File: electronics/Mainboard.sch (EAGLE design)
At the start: 225 parts, among them J1 JST_PH_B3B-PH-K-S(LF)(SN), J10 JST_PH_B3B-PH-K-S(LF)(SN), J11 JST_PH_B3B-PH-K-S(LF)(SN), J12 JST_PH_B3B-PH-K-S(LF)(SN), J13 JST_PH_B3B-PH-K-S(LF)(SN), J14 JST_PH_B3B-PH-K-S(LF)(SN), J15 JST_PH_B3B-PH-K-S(LF)(SN), J16 JST_PH_B3B-PH-K-S(LF)(SN), J17 JST_PH_B3B-PH-K-S(LF)(SN), J18 JST_PH_B3B-PH-K-S(LF)(SN), J19 JST_PH_B3B-PH-K-S(LF)(SN), J2 JST_PH_B3B-PH-K-S(LF)(SN), J20 JST_PH_B3B-PH-K-S(LF)(SN), J21 JST_PH_B3B-PH-K-S(LF)(SN), J22 JST_PH_B3B-PH-K-S(LF)(SN), J23 JST_PH_B3B-PH-K-S(LF)(SN), J24 JST_PH_B3B-PH-K-S(LF)(SN), J25 JST_PH_B3B-PH-K-S(LF)(SN), J26 JST_PH_B3B-PH-K-S(LF)(SN), J27 JST_PH_B3B-PH-K-S(LF)(SN), J28 JST_PH_B3B-PH-K-S(LF)(SN), J29 JST_PH_B3B-PH-K-S(LF)(SN), J3 JST_PH_B3B-PH-K-S(LF)(SN), J30 JST_PH_B3B-PH-K-S(LF)(SN), J31 JST_PH_B3B-PH-K-S(LF)(SN), J32 JST_PH_B3B-PH-K-S(LF)(SN), J33 B4B-PH-K-S(LF)(SN), J34 B4B-PH-K-S(LF)(SN), J35 B4B-PH-K-S(LF)(SN), J36 B4B-PH-K-S(LF)(SN), J37 B4B-PH-K-S(LF)(SN), J38 B4B-PH-K-S(LF)(SN), J39 B4B-PH-K-S(LF)(SN), J4 JST_PH_B3B-PH-K-S(LF)(SN), J40 B4B-PH-K-S(LF)(SN), J41 B4B-PH-K-S(LF)(SN), J42 B4B-PH-K-S(LF)(SN), J43 B4B-PH-K-S(LF)(SN), J44 B4B-PH-K-S(LF)(SN), J45 B4B-PH-K-S(LF)(SN), J46 B4B-PH-K-S(LF)(SN), J47 B4B-PH-K-S(LF)(SN), J48 B4B-PH-K-S(LF)(SN), J49 B4B-PH-K-S(LF)(SN), J5 JST_PH_B3B-PH-K-S(LF)(SN), J50 B4B-PH-K-S(LF)(SN), J51 B4B-PH-K-S(LF)(SN), J52 B4B-PH-K-S(LF)(SN), J53 B4B-PH-K-S(LF)(SN), J54 B4B-PH-K-S(LF)(SN), J55 B4B-PH-K-S(LF)(SN), J56 B4B-PH-K-S(LF)(SN), J57 B4B-PH-K-S(LF)(SN), J58 B4B-PH-K-S(LF)(SN), J59 B4B-PH-K-S(LF)(SN), J6 JST_PH_B3B-PH-K-S(LF)(SN), J60 B4B-PH-K-S(LF)(SN), J61 B4B-PH-K-S(LF)(SN), J62 B4B-PH-K-S(LF)(SN), J63 B4B-PH-K-S(LF)(SN), J64 B4B-PH-K-S(LF)(SN), J7 JST_PH_B3B-PH-K-S(LF)(SN), J8 JST_PH_B3B-PH-K-S(LF)(SN), J9 JST_PH_B3B-PH-K-S(LF)(SN), U1 AMP-5103309-7-34PIN_5103309-7, U15 AD5360BSTZ, U16 ADR425ARZ, U18 AD7730BRUZ, U19 AD5360BSTZ, U2 AMP-5103309-7-34PIN_5103309-7, U20 ADR425ARZ, U21 AD7730BRUZ, U22 STM32F103RCT6, U23 AD7730BRUZ, U24 AD7730BRUZ, U25 AD7730BRUZ, U26 AD7730BRUZ, U27 AD7730BRUZ, U28 AD7730BRUZ, U38 AD7730BRUZ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

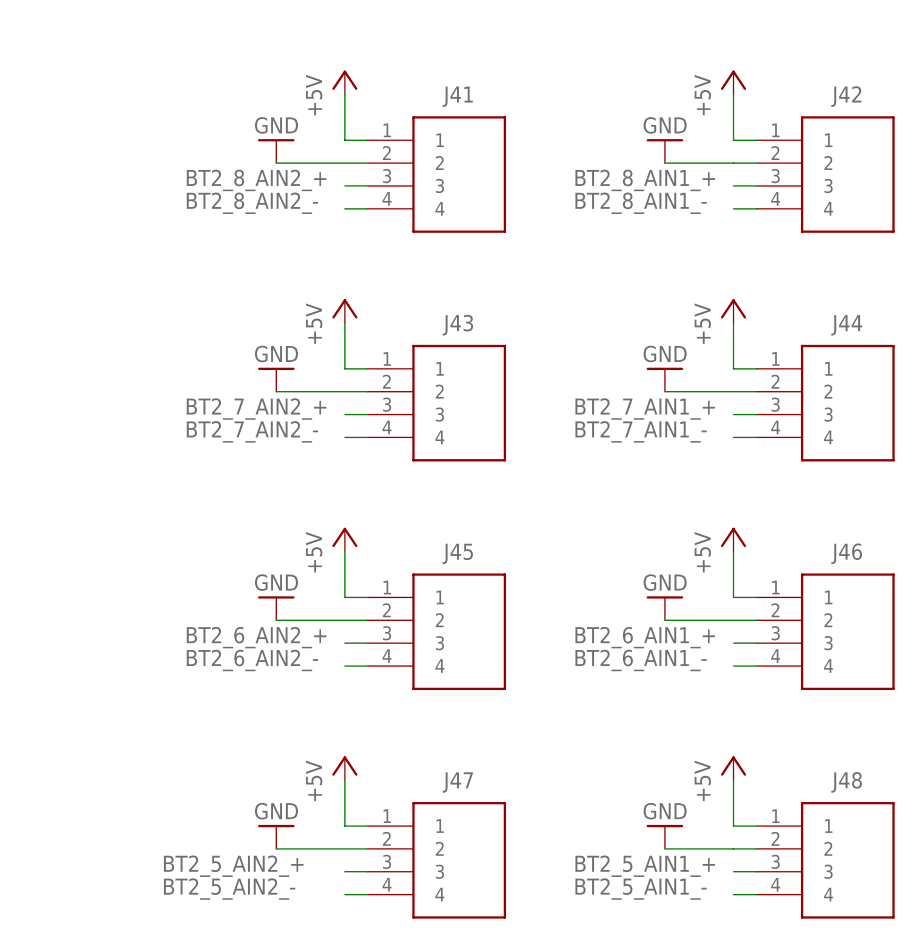
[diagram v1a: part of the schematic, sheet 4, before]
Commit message: reworked second load cell section
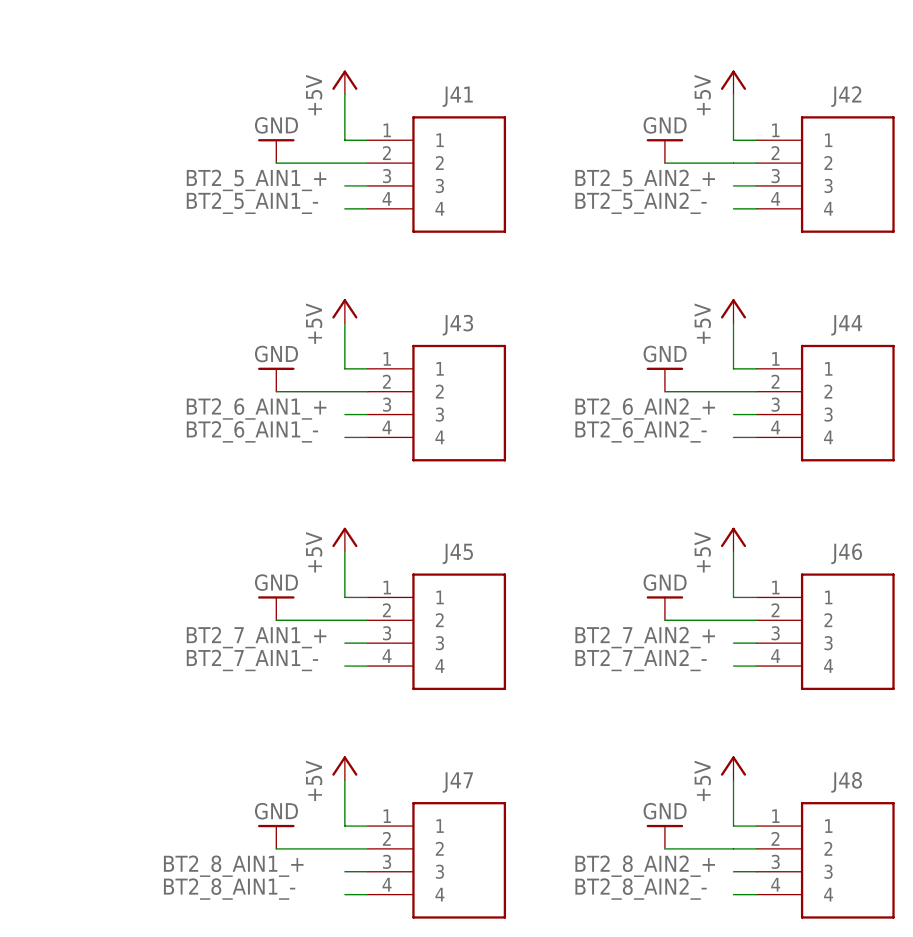
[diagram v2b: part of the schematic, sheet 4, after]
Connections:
- net N$109 renamed LC2_OSC_IN
- net N$110 renamed LC2_OSC_OUT
- net BT2_5_AIN1_+: now also J41.3; no longer J48.3
- net BT2_5_AIN1_-: now also J41.4; no longer J48.4
- net BT2_5_AIN2_+: now also J42.3; no longer J47.3
- net BT2_5_AIN2_-: now also J42.4; no longer J47.4
- net BT2_6_AIN1_+: now also J43.3; no longer J46.3
- net BT2_6_AIN1_-: now also J43.4; no longer J46.4
- net BT2_6_AIN2_+: now also J44.3; no longer J45.3
- net BT2_6_AIN2_-: now also J44.4; no longer J45.4
- net BT2_7_AIN1_+: now also J45.3; no longer J44.3
- net BT2_7_AIN1_-: now also J45.4; no longer J44.4
- net BT2_7_AIN2_+: now also J46.3; no longer J43.3
- net BT2_7_AIN2_-: now also J46.4; no longer J43.4
- net BT2_8_AIN1_+: now also J47.3; no longer J42.3
- net BT2_8_AIN1_-: now also J47.4; no longer J42.4
- net BT2_8_AIN2_+: now also J48.3; no longer J41.3
- net BT2_8_AIN2_-: now also J48.4; no longer J41.4
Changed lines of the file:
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@@
 <wire x1="121.92" y1="127" x2="129.54" y2="127" width="0.1524" layer="91"/>
 <wire x1="121.92" y1="129.54" x2="114.3" y2="129.54" width="0.1524" layer="91"/>
-<label x="73.66" y="129.54" size="1.778" layer="95"/>
+<label x="81.28" y="129.54" size="1.778" layer="95"/>
 <pinref part="C13" gate="G$1" pin="1"/>
 <wire x1="114.3" y1="129.54" x2="104.14" y2="129.54" width="0.1524" layer="91"/>
@@
 <pinref part="U22" gate="A" pin="VDDA"/>
 <wire x1="129.54" y1="137.16" x2="111.76" y2="137.16" width="0.1524" layer="91"/>
-<label x="91.44" y="137.16" size="1.778" layer="95"/>
+<label x="99.06" y="137.16" size="1.778" layer="95"/>
 <pinref part="C12" gate="G$1" pin="2"/>
 <wire x1="111.76" y1="137.16" x2="99.06" y2="137.16" width="0.1524" layer="91"/>
@@
 <wire x1="767.08" y1="137.16" x2="774.7" y2="137.16" width="0.1524" layer="91"/>
 <wire x1="767.08" y1="139.7" x2="759.46" y2="139.7" width="0.1524" layer="91"/>
-<label x="718.82" y="139.7" size="1.778" layer="95"/>
+<label x="726.44" y="139.7" size="1.778" layer="95"/>
 <pinref part="C54" gate="G$1" pin="1"/>
 <wire x1="759.46" y1="139.7" x2="749.3" y2="139.7" width="0.1524" layer="91"/>
@@
 <pinref part="U40" gate="A" pin="VDDA"/>
 <wire x1="774.7" y1="147.32" x2="756.92" y2="147.32" width="0.1524" layer="91"/>
-<label x="736.6" y="147.32" size="1.778" layer="95"/>
+<label x="744.22" y="147.32" size="1.778" layer="95"/>
 <pinref part="C53" gate="G$1" pin="2"/>
 <wire x1="756.92" y1="147.32" x2="744.22" y2="147.32" width="0.1524" layer="91"/>
@@
 </segment>
 </net>
-<net name="N$109" class="0">
+<net name="LC2_OSC_IN" class="0">
 <segment>
 <pinref part="Y8" gate="G$1" pin="OSC1"/>
@@
 <pinref part="C59" gate="G$1" pin="1"/>
 <wire x1="873.76" y1="154.94" x2="886.46" y2="154.94" width="0.1524" layer="91"/>
+<label x="835.66" y="142.24" size="1.778" layer="95"/>
 </segment>
 </net>
-<net name="N$110" class="0">
+<net name="LC2_OSC_OUT" class="0">
 <segment>
 <pinref part="Y8" gate="G$1" pin="OSC2"/>
@@
 <wire x1="904.24" y1="129.54" x2="904.24" y2="137.16" width="0.1524" layer="91"/>
 <junction x="904.24" y="137.16"/>
+<label x="835.66" y="139.7" size="1.778" layer="95"/>
 </segment>
 </net>
@@
 </segment>
 </net>
-<net name="BT2_8_AIN1_+" class="0">
-<segment>
-<pinref part="J42" gate="G$1" pin="3"/>
-<wire x1="345.44" y1="78.74" x2="342.9" y2="78.74" width="0.1524" layer="91"/>
-<label x="325.12" y="78.74" size="1.778" layer="95"/>
-</segment>
-</net>
-<net name="BT2_8_AIN1_-" class="0">
-<segment>
-<pinref part="J42" gate="G$1" pin="4"/>
-<wire x1="345.44" y1="76.2" x2="342.9" y2="76.2" width="0.1524" layer="91"/>
-<label x="325.12" y="76.2" size="1.778" layer="95"/>
-</segment>
-</net>
-<net name="BT2_8_AIN2_+" class="0">
-<segment>
-<pinref part="J41" gate="G$1" pin="3"/>
-<wire x1="302.26" y1="78.74" x2="299.72" y2="78.74" width="0.1524" layer="91"/>
-<label x="281.94" y="78.74" size="1.778" layer="95"/>
-</segment>
-</net>
-<net name="BT2_8_AIN2_-" class="0">
-<segment>
-<pinref part="J41" gate="G$1" pin="4"/>
-<wire x1="302.26" y1="76.2" x2="299.72" y2="76.2" width="0.1524" layer="91"/>
-<label x="281.94" y="76.2" size="1.778" layer="95"/>
-</segment>
-</net>
-<net name="BT2_7_AIN2_+" class="0">
-<segment>
-<pinref part="J43" gate="G$1" pin="3"/>
-<wire x1="302.26" y1="53.34" x2="299.72" y2="53.34" width="0.1524" layer="91"/>
-<label x="281.94" y="53.34" size="1.778" layer="95"/>
-</segment>
-</net>
-<net name="BT2_7_AIN2_-" class="0">
-<segment>
-<pinref part="J43" gate="G$1" pin="4"/>
-<wire x1="302.26" y1="50.8" x2="299.72" y2="50.8" width="0.1524" layer="91"/>
-<label x="281.94" y="50.8" size="1.778" layer="95"/>
-</segment>
-</net>
 <net name="BT2_6_AIN2_+" class="0">
 <segment>
-<pinref part="J45" gate="G$1" pin="3"/>
-<wire x1="302.26" y1="27.94" x2="299.72" y2="27.94" width="0.1524" layer="91"/>
-<label x="281.94" y="27.94" size="1.778" layer="95"/>
-</segment>
-</net>
-<net name="BT2_6_AIN2_-" class="0">
-<segment>
-<pinref part="J45" gate="G$1" pin="4"/>
-<wire x1="302.26" y1="25.4" x2="299.72" y2="25.4" width="0.1524" layer="91"/>
-<label x="281.94" y="25.4" size="1.778" layer="95"/>
-</segment>
-</net>
-<net name="BT2_7_AIN1_+" class="0">
-<segment>
 <pinref part="J44" gate="G$1" pin="3"/>
 <wire x1="345.44" y1="53.34" x2="342.9" y2="53.34" width="0.1524" layer="91"/>
@@
 </segment>
 </net>
-<net name="BT2_7_AIN1_-" class="0">
+<net name="BT2_6_AIN2_-" class="0">
 <segment>
 <pinref part="J44" gate="G$1" pin="4"/>
@@
 <net name="BT2_6_AIN1_+" class="0">
 <segment>
-<pinref part="J46" gate="G$1" pin="3"/>
-<wire x1="345.44" y1="27.94" x2="342.9" y2="27.94" width="0.1524" layer="91"/>
-<label x="325.12" y="27.94" size="1.778" layer="95"/>
+<pinref part="J43" gate="G$1" pin="3"/>
+<wire x1="302.26" y1="53.34" x2="299.72" y2="53.34" width="0.1524" layer="91"/>
+<label x="281.94" y="53.34" size="1.778" layer="95"/>
 </segment>
 </net>
 <net name="BT2_6_AIN1_-" class="0">
 <segment>
-<pinref part="J46" gate="G$1" pin="4"/>
-<wire x1="345.44" y1="25.4" x2="342.9" y2="25.4" width="0.1524" layer="91"/>
-<label x="325.12" y="25.4" size="1.778" layer="95"/>
+<pinref part="J43" gate="G$1" pin="4"/>
+<wire x1="302.26" y1="50.8" x2="299.72" y2="50.8" width="0.1524" layer="91"/>
+<label x="281.94" y="50.8" size="1.778" layer="95"/>
 </segment>
 </net>
 <net name="BT2_5_AIN2_+" class="0">
 <segment>
-<pinref part="J47" gate="G$1" pin="3"/>
-<wire x1="302.26" y1="2.54" x2="299.72" y2="2.54" width="0.1524" layer="91"/>
-<label x="279.4" y="2.54" size="1.778" layer="95"/>
+<pinref part="J42" gate="G$1" pin="3"/>
+<wire x1="345.44" y1="78.74" x2="342.9" y2="78.74" width="0.1524" layer="91"/>
+<label x="325.12" y="78.74" size="1.778" layer="95"/>
 </segment>
 </net>
 <net name="BT2_5_AIN2_-" class="0">
 <segment>
-<pinref part="J47" gate="G$1" pin="4"/>
-<wire x1="302.26" y1="0" x2="299.72" y2="0" width="0.1524" layer="91"/>
-<label x="279.4" y="0" size="1.778" layer="95"/>
+<pinref part="J42" gate="G$1" pin="4"/>
+<wire x1="345.44" y1="76.2" x2="342.9" y2="76.2" width="0.1524" layer="91"/>
+<label x="325.12" y="76.2" size="1.778" layer="95"/>
 </segment>
 </net>
 <net name="BT2_5_AIN1_+" class="0">
 <segment>
-<pinref part="J48" gate="G$1" pin="3"/>
-<wire x1="345.44" y1="2.54" x2="342.9" y2="2.54" width="0.1524" layer="91"/>
-<label x="325.12" y="2.54" size="1.778" layer="95"/>
+<pinref part="J41" gate="G$1" pin="3"/>
+<wire x1="302.26" y1="78.74" x2="299.72" y2="78.74" width="0.1524" layer="91"/>
+<label x="281.94" y="78.74" size="1.778" layer="95"/>
 </segment>
 </net>
 <net name="BT2_5_AIN1_-" class="0">
 <segment>
-<pinref part="J48" gate="G$1" pin="4"/>
-<wire x1="345.44" y1="0" x2="342.9" y2="0" width="0.1524" layer="91"/>
-<label x="325.12" y="0" size="1.778" layer="95"/>
+<pinref part="J41" gate="G$1" pin="4"/>
+<wire x1="302.26" y1="76.2" x2="299.72" y2="76.2" width="0.1524" layer="91"/>
+<label x="281.94" y="76.2" size="1.778" layer="95"/>
 </segment>
 </net>
@@
 </segment>
 </net>
+<net name="BT2_7_AIN1_+" class="0">
+<segment>
+<pinref part="J45" gate="G$1" pin="3"/>
+<wire x1="302.26" y1="27.94" x2="299.72" y2="27.94" width="0.1524" layer="91"/>
+<label x="281.94" y="27.94" size="1.778" layer="95"/>
+</segment>
+</net>
+<net name="BT2_7_AIN1_-" class="0">
+<segment>
+<pinref part="J45" gate="G$1" pin="4"/>
+<wire x1="302.26" y1="25.4" x2="299.72" y2="25.4" width="0.1524" layer="91"/>
+<label x="281.94" y="25.4" size="1.778" layer="95"/>
+</segment>
+</net>
+<net name="BT2_7_AIN2_-" class="0">
+<segment>
+<pinref part="J46" gate="G$1" pin="4"/>
+<wire x1="345.44" y1="25.4" x2="342.9" y2="25.4" width="0.1524" layer="91"/>
+<label x="325.12" y="25.4" size="1.778" layer="95"/>
+</segment>
+</net>
+<net name="BT2_7_AIN2_+" class="0">
+<segment>
+<pinref part="J46" gate="G$1" pin="3"/>
+<wire x1="345.44" y1="27.94" x2="342.9" y2="27.94" width="0.1524" layer="91"/>
+<label x="325.12" y="27.94" size="1.778" layer="95"/>
+</segment>
+</net>
+<net name="BT2_8_AIN1_+" class="0">
+<segment>
+<pinref part="J47" gate="G$1" pin="3"/>
+<wire x1="302.26" y1="2.54" x2="299.72" y2="2.54" width="0.1524" layer="91"/>
+<label x="279.4" y="2.54" size="1.778" layer="95"/>
+</segment>
+</net>
+<net name="BT2_8_AIN1_-" class="0">
+<segment>
+<pinref part="J47" gate="G$1" pin="4"/>
+<wire x1="302.26" y1="0" x2="299.72" y2="0" width="0.1524" layer="91"/>
+<label x="279.4" y="0" size="1.778" layer="95"/>
+</segment>
+</net>
+<net name="BT2_8_AIN2_+" class="0">
+<segment>
+<pinref part="J48" gate="G$1" pin="3"/>
+<wire x1="345.44" y1="2.54" x2="342.9" y2="2.54" width="0.1524" layer="91"/>
+<label x="325.12" y="2.54" size="1.778" layer="95"/>
+</segment>
+</net>
+<net name="BT2_8_AIN2_-" class="0">
+<segment>
+<pinref part="J48" gate="G$1" pin="4"/>
+<wire x1="345.44" y1="0" x2="342.9" y2="0" width="0.1524" layer="91"/>
+<label x="325.12" y="0" size="1.778" layer="95"/>
+</segment>
+</net>

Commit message: load cell sections done
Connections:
- net LC2_OSC_IN renamed LC_2_OSC_IN
- net LC2_OSC_OUT renamed LC_2_OSC_OUT
- removed net LC_1_RDY8: U22.PA0-WKUP, U28.*RDY
- removed net LC_1_SS1: U18.*CS, U22.PC9
- removed net LC_1_SS2: U21.*CS, U22.PC8
- removed net LC_1_SS3: U22.PC7, U23.*CS
- removed net LC_1_SS4: U22.PC6, U24.*CS
- removed net LC_1_SS5: U22.PC3, U25.*CS
- removed net LC_1_SS6: U22.PC2, U26.*CS
- removed net LC_1_SS7: U22.PC1, U27.*CS
- removed net LC_1_SS8: U22.PC0, U28.*CS
- removed net LC_2_RDY8: U40.PA0-WKUP, U46.*RDY
- removed net LC_2_SS1: U38.*CS, U40.PC9
- removed net LC_2_SS2: U39.*CS, U40.PC8
- removed net LC_2_SS3: U40.PC7, U41.*CS
- removed net LC_2_SS4: U40.PC6, U42.*CS
- removed net LC_2_SS5: U40.PC3, U43.*CS
- removed net LC_2_SS6: U40.PC2, U44.*CS
- removed net LC_2_SS7: U40.PC1, U45.*CS
- removed net LC_2_SS8: U40.PC0, U46.*CS
- new net LC_1_CS0: U18.*CS, U22.PA0-WKUP
- new net LC_1_CS1: U21.*CS, U22.PA1
- new net LC_1_CS2: U22.PA2, U23.*CS
- new net LC_1_CS3: U22.PC4, U24.*CS
- new net LC_1_CS4: U22.PC5, U25.*CS
- new net LC_1_CS5: U22.PB0, U26.*CS
- new net LC_1_CS6: U22.PB1, U27.*CS
- new net LC_1_CS7: U22.PB1_2, U28.*CS
- new net LC_1_PB7: U22.PB7
- new net LC_1_RDY0: U18.*RDY, U22.PA12
- new net LC_2_CS0: U38.*CS, U40.PA0-WKUP
- new net LC_2_CS1: U39.*CS, U40.PA1
- new net LC_2_CS2: U40.PA2, U41.*CS
- new net LC_2_CS3: U40.PC4, U42.*CS
- new net LC_2_CS4: U40.PC5, U43.*CS
- new net LC_2_CS5: U40.PB0, U44.*CS
- new net LC_2_CS6: U40.PB1, U45.*CS
- new net LC_2_CS7: U40.PB1_2, U46.*CS
- new net LC_2_PB7: U40.PB7
- new net LC_2_RDY0: U38.*RDY, U40.PA12
- net LC_1_RDY1: now also U21.*RDY; no longer U18.*RDY
- net LC_1_RDY2: now also U23.*RDY; no longer U21.*RDY
- net LC_1_RDY3: now also U24.*RDY; no longer U23.*RDY
- net LC_1_RDY4: now also U22.PA8, U25.*RDY; no longer U22.PA12, U24.*RDY
- net LC_1_RDY5: now also U22.PC9, U26.*RDY; no longer U22.PA3, U25.*RDY
- net LC_1_RDY6: now also U22.PC8, U27.*RDY; no longer U22.PA2, U26.*RDY
- net LC_1_RDY7: now also U22.PC7, U28.*RDY; no longer U22.PA1, U27.*RDY
- net LC_2_RDY1: now also U39.*RDY; no longer U38.*RDY
- net LC_2_RDY2: now also U41.*RDY; no longer U39.*RDY
- net LC_2_RDY3: now also U42.*RDY; no longer U41.*RDY
- net LC_2_RDY4: now also U40.PA8, U43.*RDY; no longer U40.PA12, U42.*RDY
- net LC_2_RDY5: now also U40.PC9, U44.*RDY; no longer U40.PA3, U43.*RDY
- net LC_2_RDY6: now also U40.PC8, U45.*RDY; no longer U40.PA2, U44.*RDY
- net LC_2_RDY7: now also U40.PC7, U46.*RDY; no longer U40.PA1, U45.*RDY

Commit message: added missing trace names
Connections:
- net N$151 renamed DAC_1_CLR
- net N$152 renamed DAC_1_RST
- net N$2 renamed PG_CURR_LIM
- net N$219 renamed DAC_2_CLR
- net N$220 renamed DAC_2_RST
- net N$3 renamed DVCC_CURR_LIM
- net N$37 renamed ADC_2_REFCAP
- net N$38 renamed ADC_2_COM_MODE
- net N$39 renamed ADC_2_RST
- net N$4 renamed +5V_CURR_LIM
- net N$40 renamed ADC_2_REFINOUT
- net N$5 renamed VDD_CURR_LIM
- net N$6 renamed HB_CURR_LIM
- net N$63 renamed ADC_2_REGCAP
- net N$64 renamed ADC_2_REGCAPD
- net N$73 renamed ADC_1_REFCAP
- net N$74 renamed ADC_1_COM_MODE
- net N$75 renamed ADC_1_RST
- net N$76 renamed ADC_1_REFINOUT
- net N$86 renamed ADC_1_REGCAP
- net N$87 renamed ADC_1_REGCAPD
- net ADC_1_VREF: now also C30.+, C66.1, C67.1, R9.2, U7.VOUT; no longer C28.+, C35.1, C36.1, R6.2, U4.VOUT
- net ADC_2_VREF: now also C28.+, C35.1, C36.1, R6.2, U4.VOUT; no longer C30.+, C66.1, C67.1, R9.2, U7.VOUT
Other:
- moved on the sheet: C45, C62, C76, C83, LED1, LED2, LED3, LED4, LED5, R2, R6, R7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

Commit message: minor changes on names and routing
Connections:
- net N$1 renamed RPI_PWR
- net N$41 renamed ADC_2_CONVST
- net N$77 renamed ADC_1_CONVST
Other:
- moved on the sheet: JP1
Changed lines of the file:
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@@
 </segment>
 </net>
-<net name="N$41" class="0">
+<net name="ADC_2_CONVST" class="0">
 <segment>
 <pinref part="U5" gate="A" pin="CONVST"/>
@@
 <wire x1="129.54" y1="45.72" x2="172.72" y2="45.72" width="0.1524" layer="91"/>
 <wire x1="172.72" y1="45.72" x2="172.72" y2="12.7" width="0.1524" layer="91"/>
+<label x="129.54" y="45.72" size="1.778" layer="95"/>
 </segment>
 </net>
@@
 </segment>
 </net>
-<net name="N$77" class="0">
+<net name="ADC_1_CONVST" class="0">
 <segment>
 <pinref part="U8" gate="A" pin="CONVST"/>
@@
 <wire x1="541.02" y1="40.64" x2="584.2" y2="40.64" width="0.1524" layer="91"/>
 <wire x1="584.2" y1="40.64" x2="584.2" y2="7.62" width="0.1524" layer="91"/>
+<label x="541.02" y="40.64" size="1.778" layer="95"/>
 </segment>
 </net>
@@
 <pinref part="C6" gate="G$1" pin="-"/>
 <junction x="104.14" y="127"/>
+<junction x="111.76" y="127"/>
 </segment>
 <segment>
@@
 <pinref part="C24" gate="G$1" pin="-"/>
 <junction x="467.36" y="121.92"/>
+<junction x="474.98" y="121.92"/>
 </segment>
 <segment>
@@
 <instance part="R10" gate="G$1" x="345.44" y="264.16" rot="R90"/>
 <instance part="P+54" gate="1" x="335.28" y="284.48"/>
-<instance part="JP1" gate="A" x="30.48" y="220.98"/>
-<instance part="P+55" gate="1" x="30.48" y="205.74" rot="R180"/>
+<instance part="JP1" gate="A" x="30.48" y="213.36"/>
+<instance part="P+55" gate="1" x="30.48" y="200.66" rot="R180"/>
 <instance part="X1" gate="-1" x="116.84" y="264.16"/>
 <instance part="X1" gate="-2" x="116.84" y="261.62"/>
@@
 <pinref part="P+55" gate="1" pin="+5V"/>
 <pinref part="JP1" gate="A" pin="1"/>
-<wire x1="30.48" y1="208.28" x2="30.48" y2="213.36" width="0.1524" layer="91"/>
+<wire x1="30.48" y1="203.2" x2="30.48" y2="205.74" width="0.1524" layer="91"/>
 </segment>
 </net>
@@
 </segment>
 </net>
-<net name="N$1" class="0">
+<net name="RPI_PWR" class="0">
 <segment>
 <pinref part="SV1" gate="G$1" pin="4"/>
@@
 <wire x1="30.48" y1="236.22" x2="30.48" y2="233.68" width="0.1524" layer="91"/>
 <pinref part="SV1" gate="G$1" pin="2"/>
-<wire x1="30.48" y1="233.68" x2="30.48" y2="228.6" width="0.1524" layer="91"/>
+<wire x1="30.48" y1="233.68" x2="30.48" y2="220.98" width="0.1524" layer="91"/>
 <wire x1="20.32" y1="233.68" x2="30.48" y2="233.68" width="0.1524" layer="91"/>
 <junction x="30.48" y="233.68"/>
 <pinref part="JP1" gate="A" pin="2"/>
+<label x="33.02" y="220.98" size="1.778" layer="95" rot="R90"/>
 </segment>
 </net>
